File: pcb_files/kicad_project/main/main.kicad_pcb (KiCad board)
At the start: 2 copper layers, 100 x 71.3 mm, 155 parts, among them IC1 AS5145B-HSST, IC2 AS5145B-HSST, J1 Conn_01x02_Socket, J2 Conn_01x04_Socket, Q1 AON7423, Y1 Crystal_GND24

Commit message: "Finaliza" (CREO) la PCB main de DragonBot2
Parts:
- removed AUX_CONN1: Conn_01x03_Pin, Connector_PinHeader_2.54mm:PinHeader_1x03_P2.54mm_Vertical
- added C13: 10uF, Capacitor_SMD:C_0805_2012Metric_Pad1.18x1.45mm_HandSolder, F.Cu at (193.2, 49.4)
- added C15: 0.1uF, Capacitor_SMD:C_0805_2012Metric_Pad1.18x1.45mm_HandSolder, F.Cu at (95.7, 49.4)
- added C17: 10uF, Capacitor_SMD:C_0805_2012Metric_Pad1.18x1.45mm_HandSolder, F.Cu at (193.1, 46.9)
- added C18: 0.1uF, Capacitor_SMD:C_0805_2012Metric_Pad1.18x1.45mm_HandSolder, F.Cu at (95.6, 47.0)
- added CONN_MORRO1: Conn_01x08_Pin, custom_footprints:DragonBot_pads_morro, F.Cu at (144.4, 63.1)
- added CSRAM1: 0.1uF, Capacitor_SMD:C_0402_1005Metric_Pad0.74x0.62mm_HandSolder, B.Cu at (144.9, 105.3)
- added MUX1: CD4051B, custom_footprints:MUX_CD4051B, F.Cu at (152.2, 67.9)
- added MUX2: CD4051B, custom_footprints:MUX_CD4051B, F.Cu at (144.4, 67.9)
- added MUX3: CD4051B, custom_footprints:MUX_CD4051B, F.Cu at (136.7, 67.9)
- added R24: 10k, Resistor_SMD:R_0402_1005Metric_Pad0.72x0.64mm_HandSolder, F.Cu at (97.4, 80.8)
- added R25: 1K, Resistor_SMD:R_0402_1005Metric_Pad0.72x0.64mm_HandSolder, F.Cu at (95.2, 63.2)
- added R26: 45, Resistor_SMD:R_0402_1005Metric_Pad0.72x0.64mm_HandSolder, F.Cu at (191.4, 81.8)
- added R27: 10k, Resistor_SMD:R_0402_1005Metric_Pad0.72x0.64mm_HandSolder, F.Cu at (191.4, 82.7)
- added R28: 45, Resistor_SMD:R_0402_1005Metric_Pad0.72x0.64mm_HandSolder, F.Cu at (97.4, 81.8)
- added R29: 10k, Resistor_SMD:R_0402_1005Metric_Pad0.72x0.64mm_HandSolder, F.Cu at (97.4, 82.7)
- added R30: 45, Resistor_SMD:R_0402_1005Metric_Pad0.72x0.64mm_HandSolder, F.Cu at (191.7, 56.8)
- added R31: 10k, Resistor_SMD:R_0402_1005Metric_Pad0.72x0.64mm_HandSolder, F.Cu at (192.8, 51.3)
- added R32: 10k, Resistor_SMD:R_0402_1005Metric_Pad0.72x0.64mm_HandSolder, F.Cu at (188.0, 54.0)
- added R33: 45, Resistor_SMD:R_0402_1005Metric_Pad0.72x0.64mm_HandSolder, F.Cu at (184.7, 63.7)
- added R34: 10k, Resistor_SMD:R_0402_1005Metric_Pad0.72x0.64mm_HandSolder, F.Cu at (186.9, 58.6)
- added R35: 10k, Resistor_SMD:R_0402_1005Metric_Pad0.72x0.64mm_HandSolder, F.Cu at (181.4, 60.2)
- added R36: 45, Resistor_SMD:R_0402_1005Metric_Pad0.72x0.64mm_HandSolder, F.Cu at (176.8, 69.3)
- added R37: 10k, Resistor_SMD:R_0402_1005Metric_Pad0.72x0.64mm_HandSolder, F.Cu at (179.7, 64.6)
- added R38: 10k, Resistor_SMD:R_0402_1005Metric_Pad0.72x0.64mm_HandSolder, F.Cu at (174.0, 65.4)
- added R39: 45, Resistor_SMD:R_0402_1005Metric_Pad0.72x0.64mm_HandSolder, F.Cu at (168.0, 73.7)
- added R40: 10k, Resistor_SMD:R_0402_1005Metric_Pad0.72x0.64mm_HandSolder, F.Cu at (171.7, 69.5)
- added R41: 10k, Resistor_SMD:R_0402_1005Metric_Pad0.72x0.64mm_HandSolder, F.Cu at (166.0, 69.4)
- added R42: 45, Resistor_SMD:R_0402_1005Metric_Pad0.72x0.64mm_HandSolder, F.Cu at (158.7, 76.7)
- added R43: 10k, Resistor_SMD:R_0402_1005Metric_Pad0.72x0.64mm_HandSolder, F.Cu at (163.0, 73.1)
- added R44: 10k, Resistor_SMD:R_0402_1005Metric_Pad0.72x0.64mm_HandSolder, F.Cu at (157.3, 72.1)
- added R45: 45, Resistor_SMD:R_0402_1005Metric_Pad0.72x0.64mm_HandSolder, F.Cu at (149.1, 78.2)
- added R46: 10k, Resistor_SMD:R_0402_1005Metric_Pad0.72x0.64mm_HandSolder, F.Cu at (153.8, 75.3)
- added R47: 10k, Resistor_SMD:R_0402_1005Metric_Pad0.72x0.64mm_HandSolder, F.Cu at (148.4, 73.4)
- added R48: 45, Resistor_SMD:R_0402_1005Metric_Pad0.72x0.64mm_HandSolder, F.Cu at (139.3, 78.1)
- added R49: 10k, Resistor_SMD:R_0402_1005Metric_Pad0.72x0.64mm_HandSolder, F.Cu at (144.4, 75.9)
- added R50: 10k, Resistor_SMD:R_0402_1005Metric_Pad0.72x0.64mm_HandSolder, F.Cu at (139.1, 73.2)
- added R51: 45, Resistor_SMD:R_0402_1005Metric_Pad0.72x0.64mm_HandSolder, F.Cu at (129.6, 76.6)
- added R52: 10k, Resistor_SMD:R_0402_1005Metric_Pad0.72x0.64mm_HandSolder, F.Cu at (135.0, 75.3)
- added R53: 10k, Resistor_SMD:R_0402_1005Metric_Pad0.72x0.64mm_HandSolder, F.Cu at (130.3, 71.7)
- added R54: 45, Resistor_SMD:R_0402_1005Metric_Pad0.72x0.64mm_HandSolder, F.Cu at (120.3, 73.5)
- added R55: 10k, Resistor_SMD:R_0402_1005Metric_Pad0.72x0.64mm_HandSolder, F.Cu at (125.8, 73.1)
- added R56: 10k, Resistor_SMD:R_0402_1005Metric_Pad0.72x0.64mm_HandSolder, F.Cu at (121.7, 68.8)
- added R57: 45, Resistor_SMD:R_0402_1005Metric_Pad0.72x0.64mm_HandSolder, F.Cu at (111.6, 69.1)
- added R58: 10k, Resistor_SMD:R_0402_1005Metric_Pad0.72x0.64mm_HandSolder, F.Cu at (117.1, 69.5)
- added R59: 10k, Resistor_SMD:R_0402_1005Metric_Pad0.72x0.64mm_HandSolder, F.Cu at (113.7, 64.6)
- added R60: 45, Resistor_SMD:R_0402_1005Metric_Pad0.72x0.64mm_HandSolder, F.Cu at (103.7, 63.4)
- added R61: 10k, Resistor_SMD:R_0402_1005Metric_Pad0.72x0.64mm_HandSolder, F.Cu at (109.1, 64.7)
- added R62: 10k, Resistor_SMD:R_0402_1005Metric_Pad0.72x0.64mm_HandSolder, F.Cu at (106.5, 59.3)
- added R63: 45, Resistor_SMD:R_0402_1005Metric_Pad0.72x0.64mm_HandSolder, F.Cu at (96.8, 56.5)
- added R64: 10k, Resistor_SMD:R_0402_1005Metric_Pad0.72x0.64mm_HandSolder, F.Cu at (101.9, 58.6)
- added R65: 10k, Resistor_SMD:R_0402_1005Metric_Pad0.72x0.64mm_HandSolder, F.Cu at (100.2, 52.9)
- added RRAM1: 10K, Resistor_SMD:R_0402_1005Metric_Pad0.72x0.64mm_HandSolder, B.Cu at (143.9, 105.3)
- added S1: ~, custom_footprints:DragonBot2_QRE1113, F.Cu at (191.2, 53.1)
- added S10: ~, custom_footprints:DragonBot2_QRE1113, F.Cu at (156.0, 74.4)
- added S11: ~, custom_footprints:DragonBot2_QRE1113, F.Cu at (151.4, 75.1)
- added S12: ~, custom_footprints:DragonBot2_QRE1113, F.Cu at (146.8, 75.5)
- added S13: ~, custom_footprints:DragonBot2_QRE1113, F.Cu at (142.0, 75.5)
- added S14: ~, custom_footprints:DragonBot2_QRE1113, F.Cu at (137.3, 75.1)
- added S15: ~, custom_footprints:DragonBot2_QRE1113, F.Cu at (132.7, 74.4)
- added S16: ~, custom_footprints:DragonBot2_QRE1113, F.Cu at (128.2, 73.3)
- added S17: ~, custom_footprints:DragonBot2_QRE1113, F.Cu at (123.7, 71.9)
- added S18: ~, custom_footprints:DragonBot2_QRE1113, F.Cu at (119.4, 70.1)
- added S19: ~, custom_footprints:DragonBot2_QRE1113, F.Cu at (115.2, 68.0)
- added S2: ~, custom_footprints:DragonBot2_QRE1113, F.Cu at (188.2, 56.6)
- added S20: ~, custom_footprints:DragonBot2_QRE1113, F.Cu at (111.3, 65.6)
- added S21: ~, custom_footprints:DragonBot2_QRE1113, F.Cu at (107.5, 62.9)
- added S22: ~, custom_footprints:DragonBot2_QRE1113, F.Cu at (103.9, 59.9)
- added S23: ~, custom_footprints:DragonBot2_QRE1113, F.Cu at (100.6, 56.6)
- added S24: ~, custom_footprints:DragonBot2_QRE1113, F.Cu at (97.5, 53.1)
- added S3: ~, custom_footprints:DragonBot2_QRE1113, F.Cu at (184.9, 59.9)
- added S4: ~, custom_footprints:DragonBot2_QRE1113, F.Cu at (181.3, 62.9)
- added S5: ~, custom_footprints:DragonBot2_QRE1113, F.Cu at (177.5, 65.6)
- added S6: ~, custom_footprints:DragonBot2_QRE1113, F.Cu at (173.5, 68.0)
- added S7: ~, custom_footprints:DragonBot2_QRE1113, F.Cu at (169.4, 70.1)
- added S8: ~, custom_footprints:DragonBot2_QRE1113, F.Cu at (165.0, 71.9)
- added S9: ~, custom_footprints:DragonBot2_QRE1113, F.Cu at (160.6, 73.3)
- added SEN_MARK_CONN_L1: Conn_01x04_Socket, custom_footprints:DragonBot_pad_marcas, F.Cu at (189.9, 107.4)
- added SEN_MARK_CONN_R1: Conn_01x04_Socket, custom_footprints:DragonBot_pad_marcas, F.Cu at (99.0, 107.4)
- added SML1: ~, custom_footprints:FujitoraBot2_QRE1113, F.Cu at (191.4, 92.8)
- added SML2: ~, custom_footprints:FujitoraBot2_QRE1113, F.Cu at (191.4, 71.1)
- added SMR1: ~, custom_footprints:FujitoraBot2_QRE1113, F.Cu at (97.4, 92.7)
- added SMR2: ~, custom_footprints:FujitoraBot2_QRE1113, F.Cu at (97.4, 71.0)
- added SRAM1: 23AA04M-I/ST, Package_SO:TSSOP-8_4.4x3mm_P0.65mm, F.Cu at (144.4, 105.3)
- added kibuzzard-696C1621: G***, kibuzzard-696C1621, F.Cu at (139.7, 107.7)
- added kibuzzard-696C163C: G***, kibuzzard-696C163C, F.Cu at (139.6, 104.6)
- added kibuzzard-696C164F: G***, kibuzzard-696C164F, F.Cu at (139.6, 101.4)
- added kibuzzard-696C1681: G***, kibuzzard-696C1681, F.Cu at (139.7, 98.3)
- added kibuzzard-696C1693: G***, kibuzzard-696C1693, F.Cu at (139.7, 95.1)
- added kibuzzard-696C16A9: G***, kibuzzard-696C16A9, F.Cu at (149.1, 95.1)
- added kibuzzard-696C16F5: G***, kibuzzard-696C16F5, F.Cu at (149.1, 98.3)
- added kibuzzard-696C171C: G***, kibuzzard-696C171C, F.Cu at (149.1, 101.5)
- added kibuzzard-696C172A: G***, kibuzzard-696C172A, F.Cu at (149.1, 104.6)
- added kibuzzard-696C173B: G***, kibuzzard-696C173B, F.Cu at (149.1, 107.7)
- ARRAY_MORRO1: footprint custom_footprints:Fujitora_pads_morro -> custom_footprints:DragonBot_pads_main
- BATT1: value Conn_01x03_Pin -> Conn_01x04_Socket; footprint Connector_JST:JST_XH_B3B-XH-A_1x03_P2.50mm_Vertical -> Connector_JST:JST_XH_B4B-XH-AM_1x04_P2.50mm_Vertical
- BUK9Q20-40H1: footprint Package_TO_SOT_SMD:SOT-23 -> custom_footprints:Mosfet_succion_BUK9Q20
- CA1, CA11, CA12, CA13, CA14, CA2, CA4, CA5, CA6, CA7, CA8, CDM10, CDM3, CDM4, CDM5, CDM8, CDM9, CIR1, CIR2, CM1, CM10, CM11, CM12, CM2, CM3, CM4, CM5, CM6, CM7, CM8, CM9, CPH4, CPH5, CPH6, CRBC1, CRBC2, CRBC3, CRBC4, R1, RBC1, RBC3, RBC4: moved to B.Cu
- CONN_ENC_L1, CONN_ENC_R1: footprint custom_footprints:FujitoraBot2_PCBmodule_encoder -> custom_footprints:DragonBot2_Encoder_main
- D11, D12: value B340 -> SS34FA; footprint Diode_SMD:D_SMC -> Diode_SMD:D_SOD-123; moved to B.Cu
- DPH1, DPH2: footprint LED_SMD:LED_0805_2012Metric -> LED_SMD:LED_0402_1005Metric_Pad0.77x0.64mm_HandSolder
- ENC_L1, ENC_R1: footprint custom_footprints:ZoroBot3_PCBmain_Encoder -> custom_footprints:DragonBot2_Encoder_main
- Q1: footprint Package_DFN_QFN:DFN-8-1EP_3x3mm_P0.65mm_EP1.55x2.4mm -> custom_footprints:AON7423
- R19: value 1K -> 10k
- SEN_MARK_L1, SEN_MARK_R1: footprint custom_footprints:ZoroBot3_Main_sensors -> custom_footprints:DragonBot_pad_marcas
- moved IC2 131.7 mm to (106.7, 83.8), turned to -90 degrees
- moved CEN4 123.8 mm to (105.6, 89.0), turned to 180 degrees
- moved CONN_ENC_R1 122.2 mm to (106.7, 91.1), turned to 90 degrees
- moved CEN3 118.2 mm to (107.8, 89.0)
- moved D15 99.5 mm to (95.2, 61.0), turned to -90 degrees
- moved D14 96.5 mm to (193.8, 61.2), turned to -90 degrees
- moved R18 95.0 mm to (193.8, 63.4), turned to 90 degrees
- moved J2 87.6 mm to (140.8, 85.7)
- moved LSM6DSR1 86.9 mm to (144.3, 85.7), turned to 90 degrees
- moved J1 86.1 mm to (147.8, 85.7), turned to 180 degrees
- moved CG2 84.0 mm to (144.3, 83.4), turned to 180 degrees
- moved ENC_L1 80.3 mm to (106.7, 123.5), turned to 180 degrees
- moved CG1 78.1 mm to (144.3, 88.0), turned to 180 degrees
- moved ENC_R1 77.3 mm to (182.1, 123.5)
- moved IC1 76.9 mm to (182.4, 83.3), turned to -90 degrees
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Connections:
- BATT1 pad 3: GND -> unconnected-(BATT1-Pin_3-Pad3)
- BUK9Q20-40H1 pad 1: /MOT_S- -> GND
- BUK9Q20-40H1 pad 2: /PWM_SUCC -> GND
- CM1 pad 1: GND -> /MOT_L-
- CM1 pad 2: /BATT -> /MOT_L+
- CM10 pad 1: GND -> /MOT_S-
- CM11 pad 1: GND -> /MOT_S-
- CM12 pad 1: GND -> /MOT_S-
- CM2 pad 1: GND -> /MOT_L-
- CM2 pad 2: /BATT -> /MOT_L+
- CM3 pad 1: GND -> /MOT_L-
- CM3 pad 2: /BATT -> /MOT_L+
- CM4 pad 1: GND -> /MOT_L-
- CM4 pad 2: /BATT -> /MOT_L+
- CM5 pad 1: GND -> /MOT_R-
- CM5 pad 2: /BATT -> /MOT_R+
- CM6 pad 1: GND -> /MOT_R-
- CM6 pad 2: /BATT -> /MOT_R+
- CM7 pad 1: GND -> /MOT_R-
- CM7 pad 2: /BATT -> /MOT_R+
- CM8 pad 1: GND -> /MOT_R-
- CM8 pad 2: /BATT -> /MOT_R+
- CM9 pad 1: GND -> /MOT_S-
- D14 pad 1: GND -> /Sensores/GND_ML
- D15 pad 1: GND -> /Sensores/GND_MR
- DEIXAME_QUE_PENSE_1 pad 2: /OUT_MUX_A -> /OUT_MUX_C
- DEIXAME_QUE_PENSE_1 pad 24: /AUX_PIN -> /NSS_SRAM
- DEIXAME_QUE_PENSE_1 pad 26: /LED8 -> /LED6
- DEIXAME_QUE_PENSE_1 pad 27: /LED9 -> /LED7
- DEIXAME_QUE_PENSE_1 pad 28: /LED10 -> /LED8
- DEIXAME_QUE_PENSE_1 pad 33: /LED7 -> /LED9
- DEIXAME_QUE_PENSE_1 pad 34: /LED6 -> /LED10
- DEIXAME_QUE_PENSE_1 pad 4: /OUT_MUX_C -> /OUT_MUX_A
- DEIXAME_QUE_PENSE_1 pad 41: /PWM_MOT_RB -> /PWM_MOT_LB
- DEIXAME_QUE_PENSE_1 pad 42: /PWM_MOT_RA -> /PWM_MOT_LA
- DEIXAME_QUE_PENSE_1 pad 43: /PWM_MOT_LB -> /PWM_MOT_RB
- DEIXAME_QUE_PENSE_1 pad 44: /PWM_MOT_LA -> /PWM_MOT_RA
- DEIXAME_QUE_PENSE_1 pad 56: /ENC_R_B -> /ENC_L_A
- DEIXAME_QUE_PENSE_1 pad 57: /ENC_R_A -> /ENC_L_B
- DEIXAME_QUE_PENSE_1 pad 58: /ENC_L_B -> /ENC_R_A
- DEIXAME_QUE_PENSE_1 pad 59: /ENC_L_A -> /ENC_R_B
- JP2 pad 1: /BATT -> Net-(JP1-A)
- JP2 pad 2: Net-(JP1-A) -> /BATT
- MP2 pad 10: /MOT_R- -> /MOT_R+
- MP2 pad 12: /MOT_R+ -> /MOT_R-
- MP2 pad 23: /MOT_R+ -> /MOT_R-
- MP2 pad 25: /MOT_R- -> /MOT_R+
- Q1 pad 1: /BATT -> Net-(JP1-A)
- Q1 pad 2: Net-(Q1-G) -> Net-(JP1-A)
- Q1 pad 4: (no net) -> Net-(Q1-G)
- Q1 pad 5: (no net) -> /BATT
- Q1 pad 6: (no net) -> /BATT
- Q1 pad 7: (no net) -> /BATT
- Q1 pad 8: (no net) -> /BATT
- R18 pad 1: +3V3 -> /Sensores/3.3_ML
- R19 pad 1: +3V3 -> /Sensores/MARK_L1
- R19 pad 2: Net-(D15-A) -> /Sensores/3.3_ML
- USB1 pad 11: +3V3 -> unconnected-(USB1-VBUS-Pad11)
- USB1 pad 2: +3V3 -> unconnected-(USB1-VBUS-Pad2)
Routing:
- net +3V3: track 0.00 -> 406.8 mm, vias 0 -> 25
- net /Sensores/3.3_M: track 0.00 -> 354.9 mm, vias 0 -> 21
- net GND: track 0.00 -> 223.3 mm, vias 0 -> 205
- net /IN_MARK_R2: track 0.00 -> 91.8 mm, vias 0 -> 3
- net /IN_MARK_R1: track 0.00 -> 87.2 mm, vias 0 -> 3
- net /PWM_MOT_RA: track 0.00 -> 71.6 mm, vias 0 -> 2
- net /PWM_MOT_RB: track 0.00 -> 69.0 mm, vias 0 -> 2
- net /IN_CURR_MR_A: track 0.00 -> 66.1 mm, vias 0 -> 4
- net /Sensores/3.3_MR: track 0.00 -> 64.0 mm, vias 0 -> 2
- net /IN_CURR_MR_B: track 0.00 -> 64.0 mm, vias 0 -> 4
- net /ENC_R_B: track 0.00 -> 62.2 mm, vias 0 -> 1
- net /ENC_R_A: track 0.00 -> 59.9 mm, vias 0 -> 1
- net /Sensores/3.3_ML: track 0.00 -> 53.1 mm, vias 0 -> 2
- net /Sensores/GND_M: track 0.00 -> 52.4 mm, vias 0 -> 29
- net /BATT_VOLTAGE: track 0.00 -> 47.7 mm, vias 0 -> 2
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- added copper zone on F.Cu, net /BATT
- added copper zone on B.Cu, net /ENC_L_GND
- added copper zone on F.Cu, net /ENC_L_GND
- added copper zone on B.Cu, net /ENC_R_GND
- added copper zone on F.Cu, net /ENC_R_GND
- added copper zone on B.Cu, net /GND_MPU
- added copper zone on F.Cu, net /GND_MPU
- added copper zone on B.Cu, net /LIPO+
- added copper zone on F.Cu, net /LIPO+
- added copper zone on B.Cu, net /MOT_L+
- added copper zone on B.Cu, net /MOT_L-
- added copper zone on B.Cu, net /MOT_R+
- added copper zone on B.Cu, net /MOT_R-
- added copper zone on B.Cu, net /MOT_S-
- added copper zone on B.Cu, net /Sensores/3.3_M
- added copper zone on F.Cu, net /Sensores/3.3_M
- added copper zone on B.Cu, net /Sensores/GND_M
- added copper zone on F.Cu, net /Sensores/GND_M
- added copper zone on B.Cu, net /Sensores/GND_ML
- added copper zone on F.Cu, net /Sensores/GND_ML
- added copper zone on B.Cu, net /Sensores/GND_MR
- added copper zone on F.Cu, net /Sensores/GND_MR
- added copper zone on B.Cu, net GND
- added copper zone on F.Cu, net GND
- added copper zone on F.Cu, net Net-(DC-DC1-SW)
- added copper zone on F.Cu, net Net-(JP1-A)
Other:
- board size 100 x 71.3 mm -> 102 x 90.8 mm

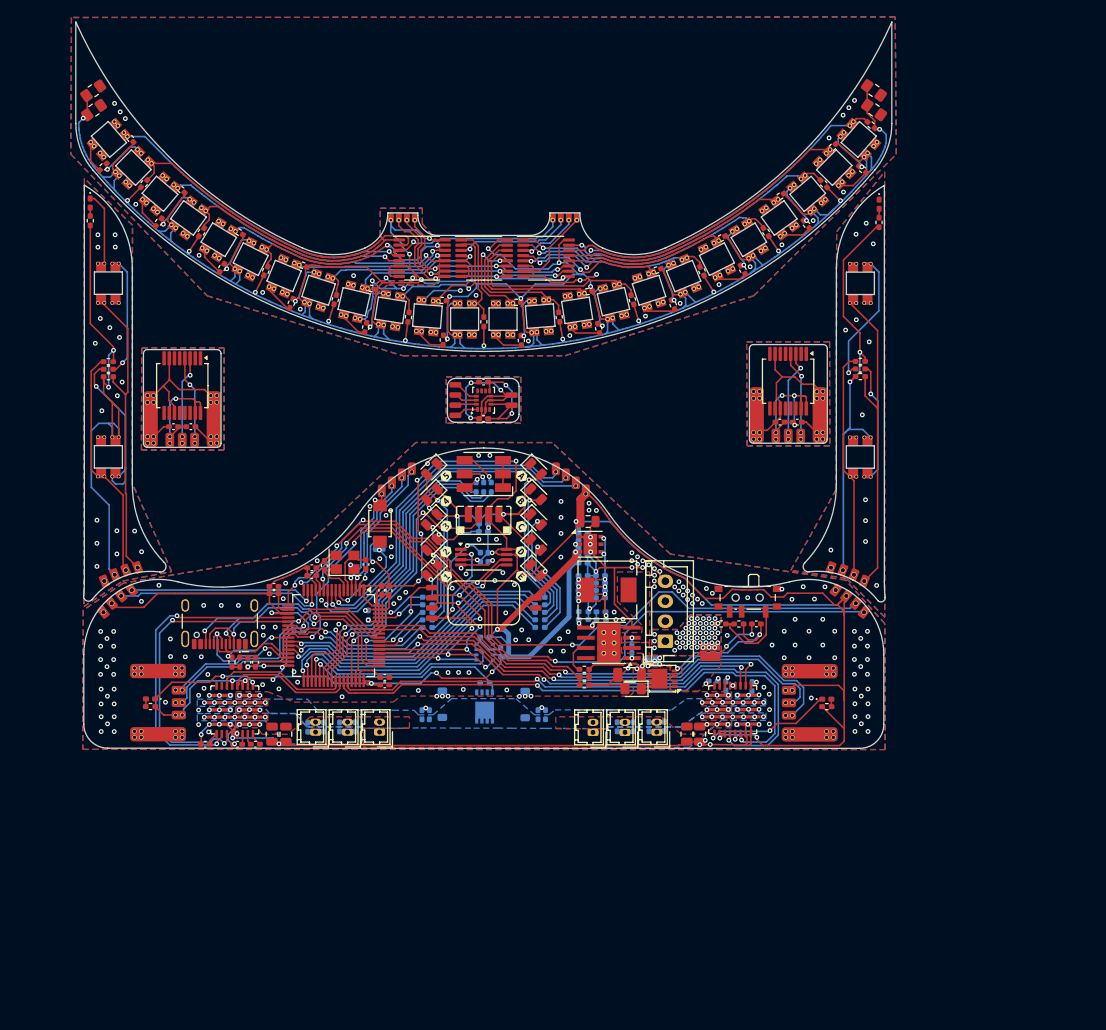
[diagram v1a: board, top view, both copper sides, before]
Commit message: Añade la PCB del chasis y revisa ajustes finales en la PCB main.
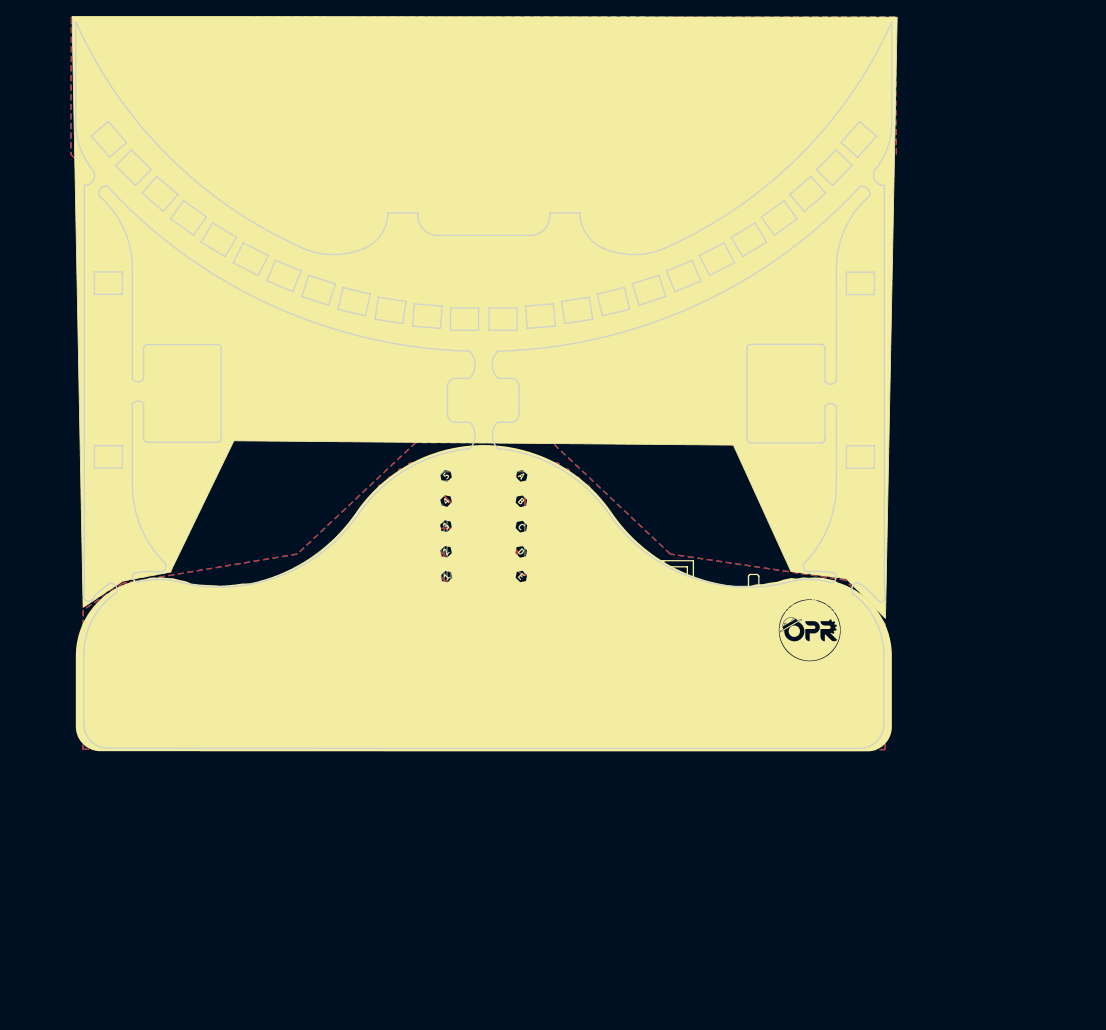
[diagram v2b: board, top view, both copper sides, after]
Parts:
- removed kibuzzard-696C1621: G***, kibuzzard-696C1621
- removed kibuzzard-696C163C: G***, kibuzzard-696C163C
- removed kibuzzard-696C164F: G***, kibuzzard-696C164F
- removed kibuzzard-696C1681: G***, kibuzzard-696C1681
- removed kibuzzard-696C1693: G***, kibuzzard-696C1693
- removed kibuzzard-696C16A9: G***, kibuzzard-696C16A9
- removed kibuzzard-696C16F5: G***, kibuzzard-696C16F5
- removed kibuzzard-696C171C: G***, kibuzzard-696C171C
- removed kibuzzard-696C172A: G***, kibuzzard-696C172A
- removed kibuzzard-696C173B: G***, kibuzzard-696C173B
- added ?: , , F.Cu at (194.6, 45.0)
- added ?: , , F.Cu at (193.6, 124.9)
- added ?: , , F.Cu at (113.7, 71.1)
- added ?: , , F.Cu at (97.9, 62.9)
- added ?: , , F.Cu at (175.2, 71.0)
- added ?: , , F.Cu at (193.6, 117.9)
- added ?: , , F.Cu at (95.2, 124.9)
- added ?: , , F.Cu at (95.2, 117.9)
- added ?: , , F.Cu at (94.2, 45.0)
- added ?: , , F.Cu at (191.0, 62.9)
- added JP99: SolderJumper_2_Open, Jumper:SolderJumper-2_P1.3mm_Open_RoundedPad1.0x1.5mm, B.Cu at (143.7, 79.1)
- moved CONN_ENC_R1 0.63 mm to (106.7, 90.4)
- moved IC2 0.63 mm to (106.7, 83.2)
- moved CEN3 0.63 mm to (107.8, 88.3)
- moved CEN4 0.63 mm to (105.6, 88.3)
- moved IC1 0.29 mm to (182.1, 83.3)
- moved CEN1 0.29 mm to (183.3, 88.4)
- moved CONN_ENC_L1 0.29 mm to (182.1, 90.5)
- moved CEN2 0.29 mm to (181.1, 88.4)
- turned POWER_MPU1 to 180 degrees
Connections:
- LSM6DSR1 pad 2: /GND_MPU -> /3.3_MPU
- LSM6DSR1 pad 3: /GND_MPU -> /3.3_MPU
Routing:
- net /GND_MPU: track 25.0 -> 18.3 mm
- net +3V3: track 406.8 -> 401.7 mm
- net /3.3_MPU: track 16.7 -> 21.4 mm
- net GND: track 223.3 -> 223.4 mm, vias 205 -> 201
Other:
- outline, holes or cut-outs redrawn

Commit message: Actualiza los archivos de la PCB a la ultima version pedida.
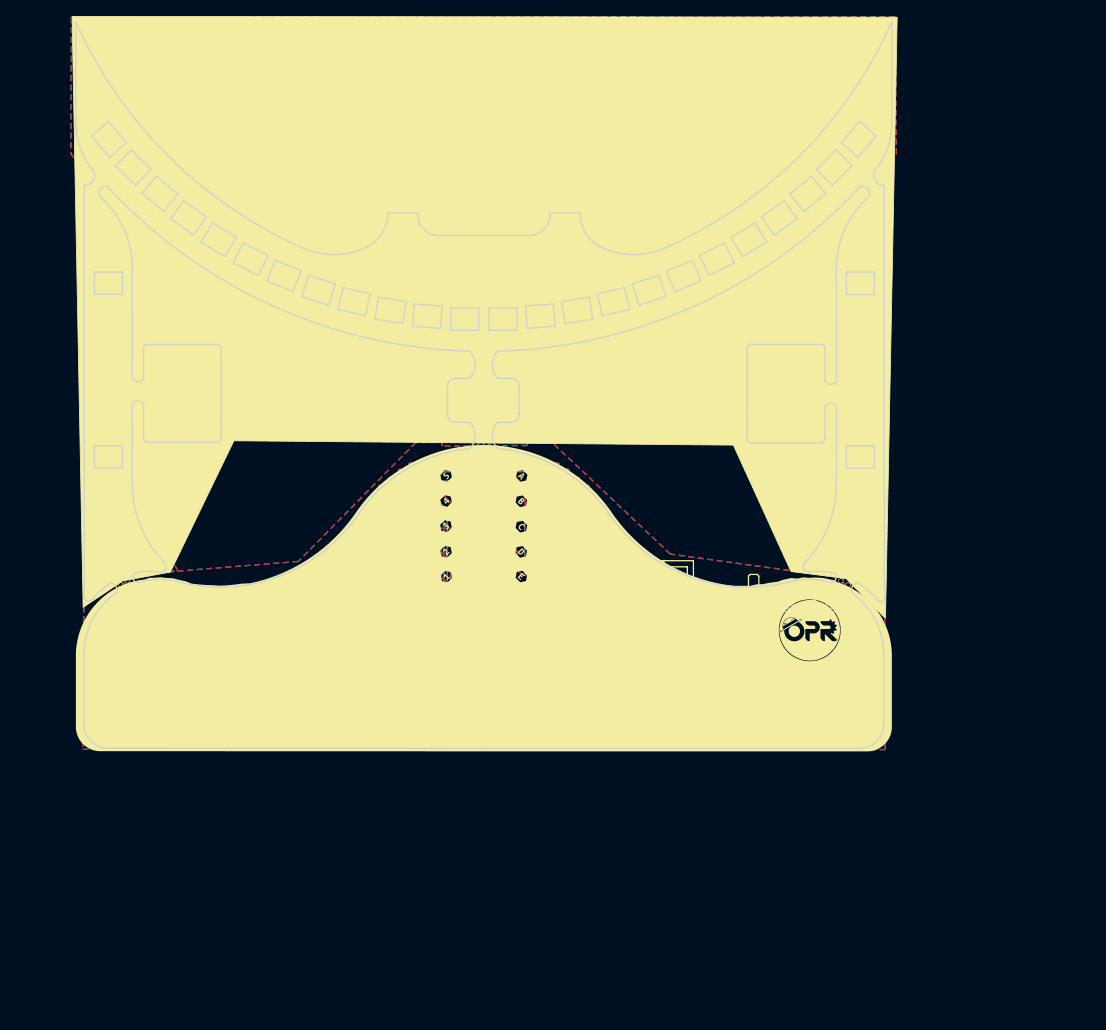
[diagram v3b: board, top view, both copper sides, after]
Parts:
- added ?: , , F.Cu at (189.9, 108.8)
- added ?: , , F.Cu at (99.8, 108.2)
- added ?: , , F.Cu at (189.0, 108.2)
- added ?: , , F.Cu at (99.0, 108.7)
- moved R45 0.13 mm to (149.2, 78.2)
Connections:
- IC1 pad 1: unconnected-(IC1-MAGINCN-Pad1) -> /Sensores/MARK_L1
- IC2 pad 8: unconnected-(IC2-PDIO-Pad8) -> /Sensores/MARK_R2
- J1 pad 1: /3.3_MPU -> +3V3
- JP99 pad 1: /Sensores/3.3_M -> /3.3_MPU
- POWER_SWITCH1 pad : (no net) -> GND
- R18 pad 1: /Sensores/3.3_ML -> /Sensores/3.3_M
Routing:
- net /BATT: track 14.4 -> 58.3 mm
- net /Sensores/3.3_M: track 354.9 -> 388.6 mm, vias 21 -> 26
- net /Sensores/MARK_L1: track 28.3 -> 49.8 mm, vias 0 -> 2
- net +3V3: track 401.7 -> 422.0 mm, vias 25 -> 26
- net /MOT_R-: track 0.00 -> 17.9 mm
- net /Sensores/MARK_R2: track 37.9 -> 54.3 mm, vias 0 -> 2
- net /MOT_R+: track 0.00 -> 15.3 mm
- net /3.3_MPU: track 21.4 -> 36.4 mm
- net /MOT_L-: track 7.61 -> 16.5 mm
- net /MOT_L+: track 7.63 -> 15.3 mm
- net /Sensores/3.3_MR: track 64.0 -> 67.1 mm
- net /PWM_MOT_RB: track 69.0 -> 71.8 mm
- net /Sensores/3.3_ML: track 53.1 -> 55.7 mm
- net /IN_MARK_L2: track 23.8 -> 24.8 mm
- net /GND_MPU: vias 3 -> 9
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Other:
- outline, holes or cut-outs redrawn
